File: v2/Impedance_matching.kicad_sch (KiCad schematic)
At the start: 13 parts

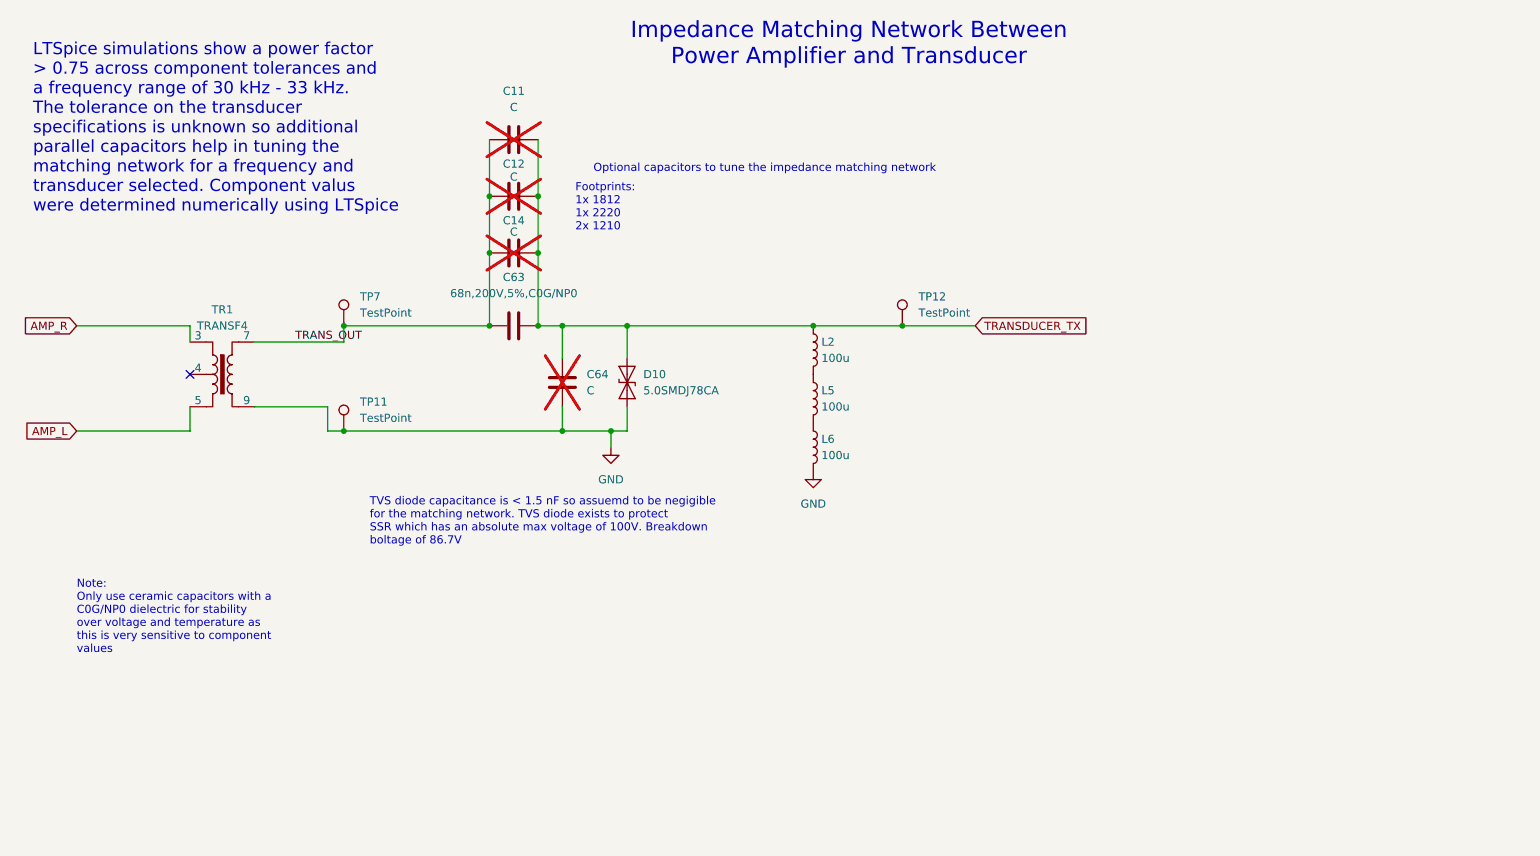
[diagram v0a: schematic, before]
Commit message: Most v2 changes made
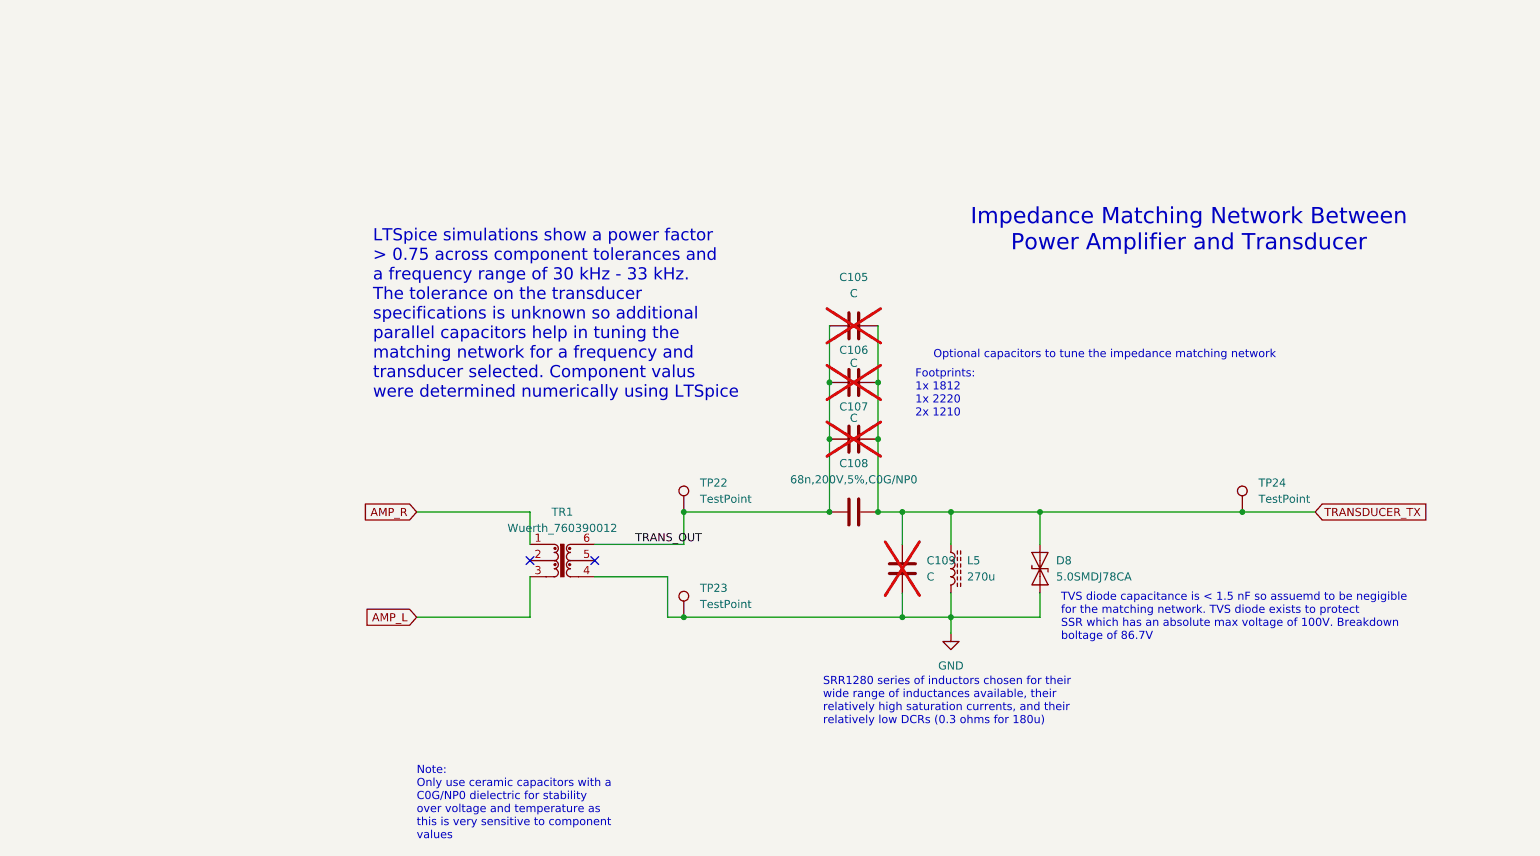
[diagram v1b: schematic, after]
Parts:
- removed C11: C, Capacitor_SMD:C_2220_5750Metric_Pad1.97x5.40mm_HandSolder, symbol UAM_symbols:C
- removed C12, C14: C, Capacitor_SMD:C_1210_3225Metric_Pad1.33x2.70mm_HandSolder, symbol UAM_symbols:C
- removed L2, L5, L6: 100u, Inductor:PA4344, symbol Device:L
- removed TR1: TRANSF4, Transformer:750315836, symbol Transformer:TRANSF4
- added C105: C, Capacitor_SMD:C_2220_5750Metric_Pad1.97x5.40mm_HandSolder, symbol UAM_symbols:C
- added C106, C107: C, Capacitor_SMD:C_1210_3225Metric_Pad1.33x2.70mm_HandSolder, symbol UAM_symbols:C
- added L5: 270u, Inductor_SMD:L_12x12mm_H8mm, symbol UAM_symbols:L_Ferrite
- added TR1: Wuerth_760390012, Transformer_SMD:Transformer_Wuerth_750315371, symbol UAM_symbols:Wuerth_750315371
- renumbered C63 to C108, C64 to C109, D10 to D8, TP7 to TP22, TP11 to TP23, TP12 to TP24
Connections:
- net AMP_L: now also TR1.3
- net AMP_R: now also TR1.1
- net GND: now also L5.2, TR1.4
- net TRANSDUCER_TX: now also C105.2, C106.2, C107.2, L5.1
- net TRANS_OUT: now also C105.1, C106.1, C107.1, TR1.6
- no-connect marks 1 -> 2
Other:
- note added: "SRR1280 series of inductors chosen for their wide range of inductances available, their relatively high saturation currents, and their relatively low DCRs (0.3 ohms for 180u)"
- company: EV -> (none)
- title: Impedance Matching Network -> (none)
- moved on the sheet: C108, C109, D8, TP22, TP23, TP24
